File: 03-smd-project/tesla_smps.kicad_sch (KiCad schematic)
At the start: 94 parts, among them J1 OUTPUT: 25.8 VDC/20 W, P1 Line1, P2 Line2, T1 2SK1317, T2 2N2222, T3 2N2222, U1 LTV-817, U2 LTV-817

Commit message: Add new PCB version and changelogs
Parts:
- C1, C9: footprint Capacitor_THT:CP_Radial_D8.0mm_P5.00mm -> Capacitor_THT:CP_Radial_D8.0mm_P3.50mm
- C15, C16, C17: footprint Capacitor_THT:C_Radial_D12.5mm_H25.0mm_P5.00mm -> Capacitor_THT:C_Radial_D16.0mm_H31.5mm_P7.50mm
- C3: footprint Capacitor_THT:C_Radial_D12.5mm_H25.0mm_P5.00mm -> Capacitor_THT:C_Radial_D16.0mm_H25.0mm_P7.50mm
- R16: footprint Resistor_THT:R_Axial_DIN0309_L9.0mm_D3.2mm_P2.54mm_Vertical -> Resistor_THT:R_Axial_DIN0614_L14.3mm_D5.7mm_P5.08mm_Vertical
- R2, R8: footprint Resistor_SMD:R_0402_1005Metric -> Resistor_SMD:R_0805_2012Metric
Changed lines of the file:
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@@
 			)
 		)
-		(property "Footprint" "Resistor_THT:R_Axial_DIN0309_L9.0mm_D3.2mm_P2.54mm_Vertical"
+		(property "Footprint" "Resistor_THT:R_Axial_DIN0614_L14.3mm_D5.7mm_P5.08mm_Vertical"
 			(at 85.852 76.2 90)
 			(effects
@@
 			)
 		)
-		(property "Datasheet" "http://www.token.com.tw/pdf/resistor/resistor-forming-dimensions.pdf"
+		(property "Datasheet" "https://br.mouser.com/datasheet/2/418/9/ENG_CD_2176612_BA1-3367925.pdf"
 			(at 87.63 76.2 0)
 			(effects
@@
 			)
 		)
-		(property "Footprint" "Capacitor_THT:C_Radial_D12.5mm_H25.0mm_P5.00mm"
+		(property "Footprint" "Capacitor_THT:C_Radial_D16.0mm_H31.5mm_P7.50mm"
 			(at 219.71 50.8 0)
 			(effects
@@
 			)
 		)
-		(property "Datasheet" "https://br.mouser.com/datasheet/2/420/United-Chemi-Con-1511408.pdf"
+		(property "Datasheet" "https://www.tdk-electronics.tdk.com/inf/20/30/db/aec_2013/B41821_B43821.pdf"
 			(at 219.71 50.8 0)
 			(effects
@@
 			)
 		)
-		(property "Footprint" "Capacitor_THT:C_Radial_D12.5mm_H25.0mm_P5.00mm"
+		(property "Footprint" "Capacitor_THT:C_Radial_D16.0mm_H31.5mm_P7.50mm"
 			(at 219.71 63.5 0)
 			(effects
@@
 			)
 		)
-		(property "Datasheet" "https://br.mouser.com/datasheet/2/420/United-Chemi-Con-1511408.pdf"
+		(property "Datasheet" "https://www.tdk-electronics.tdk.com/inf/20/30/db/aec_2013/B41821_B43821.pdf"
 			(at 219.71 63.5 0)
 			(effects
@@
 			)
 		)
-		(property "Footprint" "Capacitor_THT:C_Radial_D12.5mm_H25.0mm_P5.00mm"
+		(property "Footprint" "Capacitor_THT:C_Radial_D16.0mm_H31.5mm_P7.50mm"
 			(at 219.71 76.2 0)
 			(effects
@@
 			)
 		)
-		(property "Datasheet" "https://br.mouser.com/datasheet/2/420/United-Chemi-Con-1511408.pdf"
+		(property "Datasheet" "https://www.tdk-electronics.tdk.com/inf/20/30/db/aec_2013/B41821_B43821.pdf"
 			(at 219.71 76.2 0)
 			(effects
@@
 			)
 		)
-		(property "Footprint" "Capacitor_THT:CP_Radial_D8.0mm_P5.00mm"
+		(property "Footprint" "Capacitor_THT:CP_Radial_D8.0mm_P3.50mm"
 			(at 69.85 90.17 0)
 			(effects
@@
 			)
 		)
-		(property "Datasheet" ""
+		(property "Datasheet" "https://br.mouser.com/datasheet/2/315/ABA0000C1215-1109177.pdf"
 			(at 69.85 90.17 0)
 			(effects
@@
 			)
 		)
-		(property "Footprint" "Capacitor_THT:C_Radial_D12.5mm_H25.0mm_P5.00mm"
+		(property "Footprint" "Capacitor_THT:C_Radial_D16.0mm_H25.0mm_P7.50mm"
 			(at 35.56 74.93 0)
 			(effects
@@
 			)
 		)
-		(property "Datasheet" "https://br.mouser.com/datasheet/2/212/KEM_A4055_ESE-1140496.pdf"
+		(property "Datasheet" "https://www.mouser.com/catalog/specsheets/tdk_b41821_b43821.pdf?_gl=1*1stbbr3*_gcl_aw*R0NMLjE3MTg2NTU2NTUuQ2owS0NRand2Yi16QmhDbUFSSXNBQWZVSTJzdjltU3NZNlZkbUxJVFV5TEVvUU13eDF5T0xuNTc1WldsWVJuZ25LaDk2WXlRcmQ2WHV6b2FBc2lURUFMd193Y0I.*_gcl_au*OTUyOTkzNzc0LjE3MTU0NTc4NDk.*_ga*MTI5ODczODI3My4xNjkwMzI0NjIw*_ga_15W4STQT4T*MTcyMjgyMTk2Ny4xMS4xLjE3MjI4MjIwMzMuNTcuMC4w"
 			(at 35.56 74.93 0)
 			(effects
@@
 			)
 		)
-		(property "Footprint" "Capacitor_THT:CP_Radial_D8.0mm_P5.00mm"
+		(property "Footprint" "Capacitor_THT:CP_Radial_D8.0mm_P3.50mm"
 			(at 17.78 115.57 0)
 			(effects
@@
 			)
 		)
-		(property "Datasheet" ""
+		(property "Datasheet" "https://br.mouser.com/datasheet/2/315/ABA0000C1215-1109177.pdf"
 			(at 17.78 115.57 0)
 			(effects
@@
 			)
 		)
-		(property "Footprint" "Resistor_SMD:R_0402_1005Metric"
+		(property "Footprint" "Resistor_SMD:R_0805_2012Metric"
 			(at 28.448 127 90)
 			(effects
@@
 			)
 		)
-		(property "Footprint" "Resistor_SMD:R_0402_1005Metric"
+		(property "Footprint" "Resistor_SMD:R_0805_2012Metric"
 			(at 57.658 124.46 90)
 			(effects

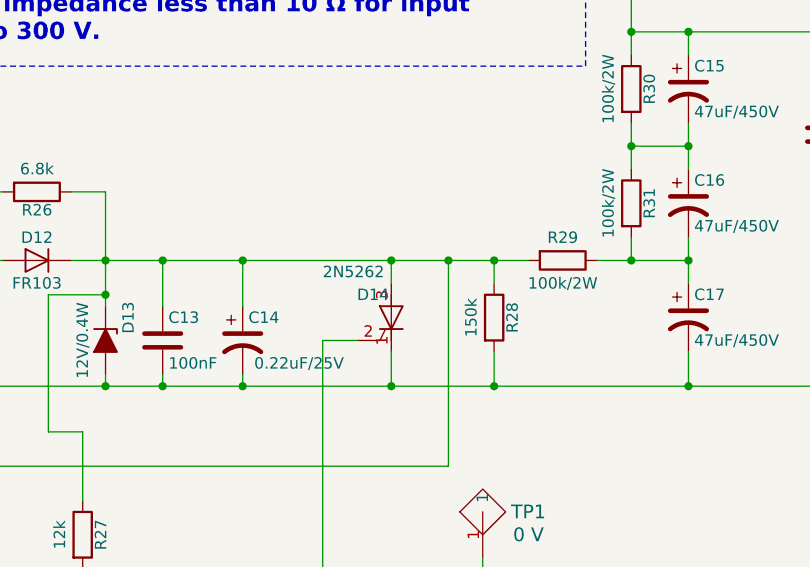
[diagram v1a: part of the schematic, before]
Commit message: Add release candidate for PCB version 1.1
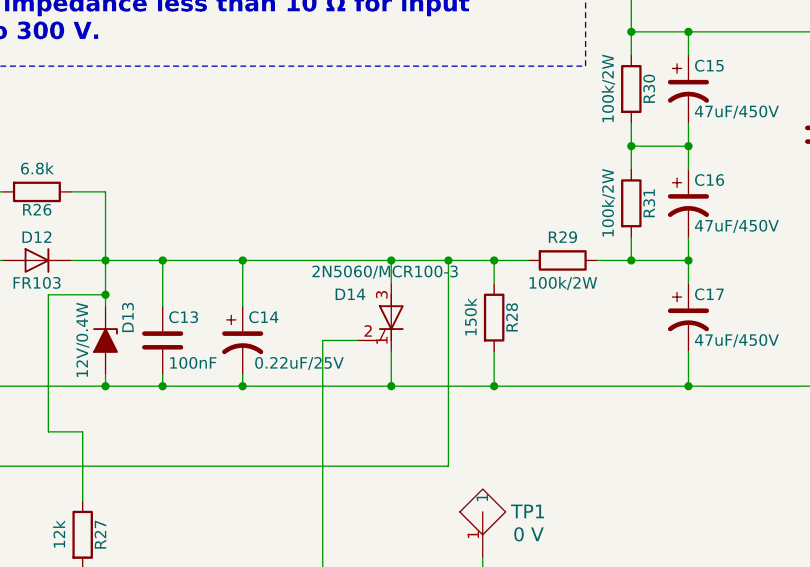
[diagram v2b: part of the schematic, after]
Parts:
- C15, C16, C17: footprint Capacitor_THT:C_Radial_D16.0mm_H31.5mm_P7.50mm -> Capacitor_THT:CP_Radial_D16.0mm_P7.50mm
- C3: footprint Capacitor_THT:C_Radial_D16.0mm_H25.0mm_P7.50mm -> Capacitor_THT:CP_Radial_D16.0mm_P7.50mm
- D14: value 2N5262 -> 2N5060/MCR100-3
- R22: footprint Resistor_SMD:R_0402_1005Metric -> Resistor_SMD:R_2010_5025Metric_Pad1.40x2.65mm_HandSolder
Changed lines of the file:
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@@
 		(comment 2 "Creative Commons")
 		(comment 3 "Wide Range and High Voltage SMPS with Flyback topology for industrial & home application")
+		(comment 4 "Rev 1.2")
 	)
 	(junction
@@
 			)
 		)
-		(property "Footprint" "Capacitor_THT:C_Radial_D16.0mm_H31.5mm_P7.50mm"
+		(property "Footprint" "Capacitor_THT:CP_Radial_D16.0mm_P7.50mm"
 			(at 219.71 50.8 0)
 			(effects
@@
 			)
 		)
-		(property "Footprint" "Capacitor_THT:C_Radial_D16.0mm_H31.5mm_P7.50mm"
+		(property "Footprint" "Capacitor_THT:CP_Radial_D16.0mm_P7.50mm"
 			(at 219.71 63.5 0)
 			(effects
@@
 			)
 		)
-		(property "Footprint" "Capacitor_THT:C_Radial_D16.0mm_H31.5mm_P7.50mm"
+		(property "Footprint" "Capacitor_THT:CP_Radial_D16.0mm_P7.50mm"
 			(at 219.71 76.2 0)
 			(effects
@@
 		(dnp no)
 		(property "Reference" "D14"
-			(at 182.88 73.66 0)
+			(at 180.34 73.66 0)
 			(effects
 				(font
@@
 			)
 		)
-		(property "Value" "2N5262"
-			(at 179.07 71.12 0)
+		(property "Value" "2N5060/MCR100-3"
+			(at 177.8 71.12 0)
 			(effects
 				(font
@@
 			)
 		)
-		(property "Footprint" "Resistor_SMD:R_0402_1005Metric"
+		(property "Footprint" "Resistor_SMD:R_2010_5025Metric_Pad1.40x2.65mm_HandSolder"
 			(at 106.68 90.932 90)
 			(effects
@@
 			)
 		)
-		(property "Footprint" "Capacitor_THT:C_Radial_D16.0mm_H25.0mm_P7.50mm"
+		(property "Footprint" "Capacitor_THT:CP_Radial_D16.0mm_P7.50mm"
 			(at 35.56 74.93 0)
 			(effects
